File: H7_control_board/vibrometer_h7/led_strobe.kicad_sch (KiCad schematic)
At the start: 15 parts, among them Q01 NPN

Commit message: worked on audio output stuff, cleaned schematic
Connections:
- net V_USB renamed +5V
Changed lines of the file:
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@@
 	(wire
 		(pts
-			(xy 56.515 64.77) (xy 56.515 67.945)
+			(xy 55.88 65.405) (xy 55.88 67.945)
 		)
 		(stroke
@@
 	(wire
 		(pts
-			(xy 56.515 67.945) (xy 64.77 67.945)
+			(xy 55.88 67.945) (xy 64.77 67.945)
 		)
 		(stroke
@@
 	)
 	(symbol
-		(lib_id "power:+5V")
-		(at 56.515 64.77 0)
-		(mirror y)
-		(unit 1)
-		(exclude_from_sim no)
-		(in_bom yes)
-		(on_board yes)
-		(dnp no)
-		(property "Reference" "#PWR062"
-			(at 56.515 68.58 0)
-			(effects
-				(font
-					(size 1.27 1.27)
-				)
-				(hide yes)
-			)
-		)
-		(property "Value" "V_USB"
-			(at 56.515 60.96 0)
-			(effects
-				(font
-					(size 1.27 1.27)
-				)
-			)
-		)
-		(property "Footprint" ""
-			(at 56.515 64.77 0)
-			(effects
-				(font
-					(size 1.27 1.27)
-				)
-				(hide yes)
-			)
-		)
-		(property "Datasheet" ""
-			(at 56.515 64.77 0)
-			(effects
-				(font
-					(size 1.27 1.27)
-				)
-				(hide yes)
-			)
-		)
-		(property "Description" "Power symbol creates a global label with name \"+5V\""
-			(at 56.515 64.77 0)
-			(effects
-				(font
-					(size 1.27 1.27)
-				)
-				(hide yes)
-			)
-		)
-		(pin "1"
-		)
-		(instances
-			(project "vibrometer_h7"
-				(path "/18de6987-156a-4b34-871e-cbbe1d261986/4fe48606-f27d-4ac1-8d68-53a5c8e78c55"
-					(reference "#PWR062")
-					(unit 1)
-				)
-			)
-		)
-	)
-	(symbol
 		(lib_id "power:GND")
 		(at 64.77 79.375 0)
@@
 					(unit 1)
 				)
+			)
+		)
+	)
+	(symbol
+		(lib_id "power:+5V")
+		(at 55.88 65.405 0)
+		(unit 1)
+		(exclude_from_sim no)
+		(in_bom yes)
+		(on_board yes)
+		(dnp no)
+		(property "Reference" "#PWR062"
+			(at 55.88 69.215 0)
+			(effects
+				(font
+					(size 1.27 1.27)
+				)
+				(hide yes)
+			)
+		)
+		(property "Value" "+5V"
+			(at 55.88 61.468 0)
+			(effects
+				(font
+					(size 1.27 1.27)
+				)
+			)
+		)
+		(property "Footprint" ""
+			(at 55.88 65.405 0)
+			(effects
+				(font
+					(size 1.27 1.27)
+				)
+				(hide yes)
+			)
+		)
+		(property "Datasheet" ""
+			(at 55.88 65.405 0)
+			(effects
+				(font
+					(size 1.27 1.27)
+				)
+				(hide yes)
+			)
+		)
+		(property "Description" "Power symbol creates a global label with name \"+5V\""
+			(at 55.88 65.405 0)
+			(effects
+				(font
+					(size 1.27 1.27)
+				)
+				(hide yes)
+			)
+		)
+		(pin "1"
+		)
+		(instances
+			(project "vibrometer_h7"
+				(path "/18de6987-156a-4b34-871e-cbbe1d261986/4fe48606-f27d-4ac1-8d68-53a5c8e78c55"
+					(reference "#PWR062")
+					(unit 1)
+				)

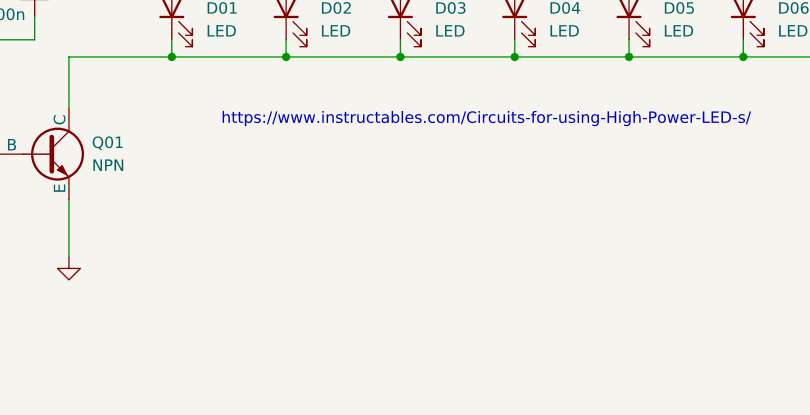
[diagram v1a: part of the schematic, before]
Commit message: added notes about LED drive component selection
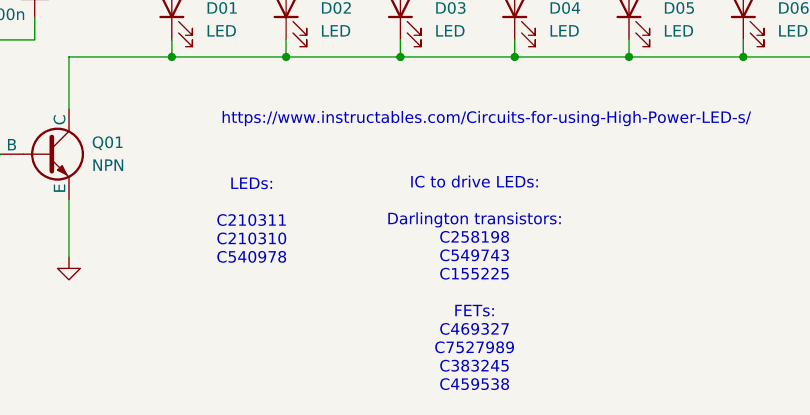
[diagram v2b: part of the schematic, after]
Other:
- note added: "IC to drive LEDs: Darlington transistors: C258198 C549743 C155225 FETs: C469327 C7527989 C383245 C459538"
- note added: "LEDs: C210311 C210310 C540978"
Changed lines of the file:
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@@
+		)
+	)
+	(text "LEDs:\n\nC210311\nC210310\nC540978\n"
+		(exclude_from_sim no)
+		(at 97.79 97.79 0)
+		(effects
+			(font
+				(size 1.27 1.27)
+			)
+		)
+	)
+	(text "IC to drive LEDs:\n\nDarlington transistors:\nC258198\nC549743\nC155225\n\nFETs:\nC469327\nC7527989\nC383245\nC459538"
+		(exclude_from_sim no)
+		(at 122.555 104.775 0)
+		(effects
+			(font
+				(size 1.27 1.27)
+			)
 		)
 	)

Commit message: started part selection
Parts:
- C01, C02: footprint (none) -> Capacitor_SMD:C_0603_1608Metric
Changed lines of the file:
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@@
 			)
 		)
-		(property "Footprint" ""
+		(property "Footprint" "Capacitor_SMD:C_0603_1608Metric"
 			(at 73.66 72.39 0)
 			(effects
@@
 			)
 		)
-		(property "Footprint" ""
+		(property "Footprint" "Capacitor_SMD:C_0603_1608Metric"
 			(at 64.77 72.39 0)
 			(effects

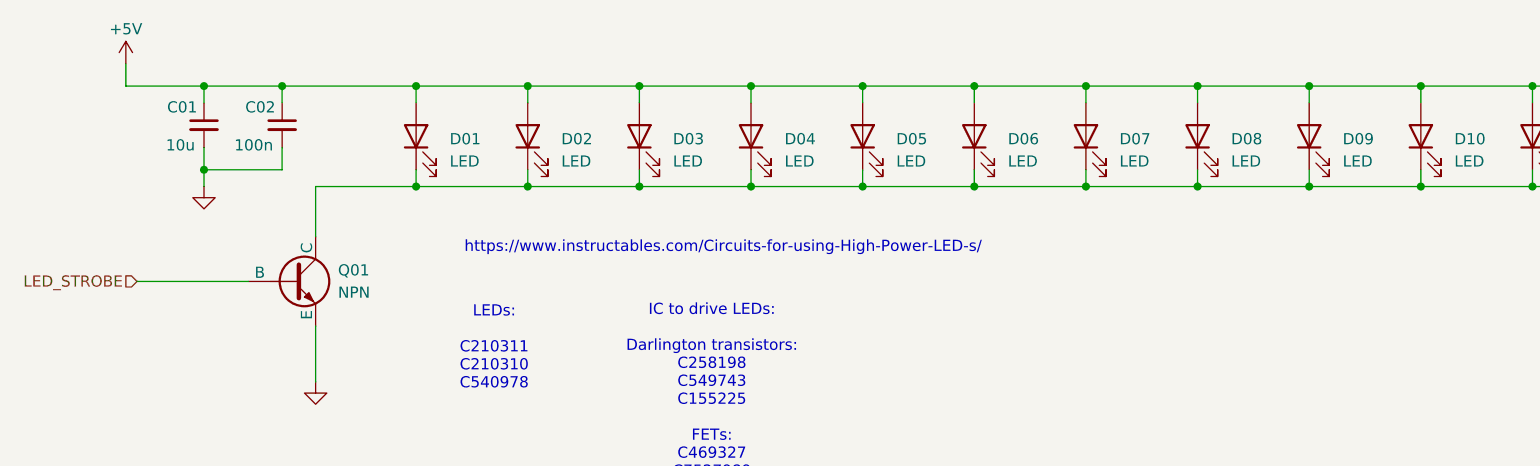
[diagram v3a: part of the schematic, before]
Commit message: component selection, headphone amp circuit specs
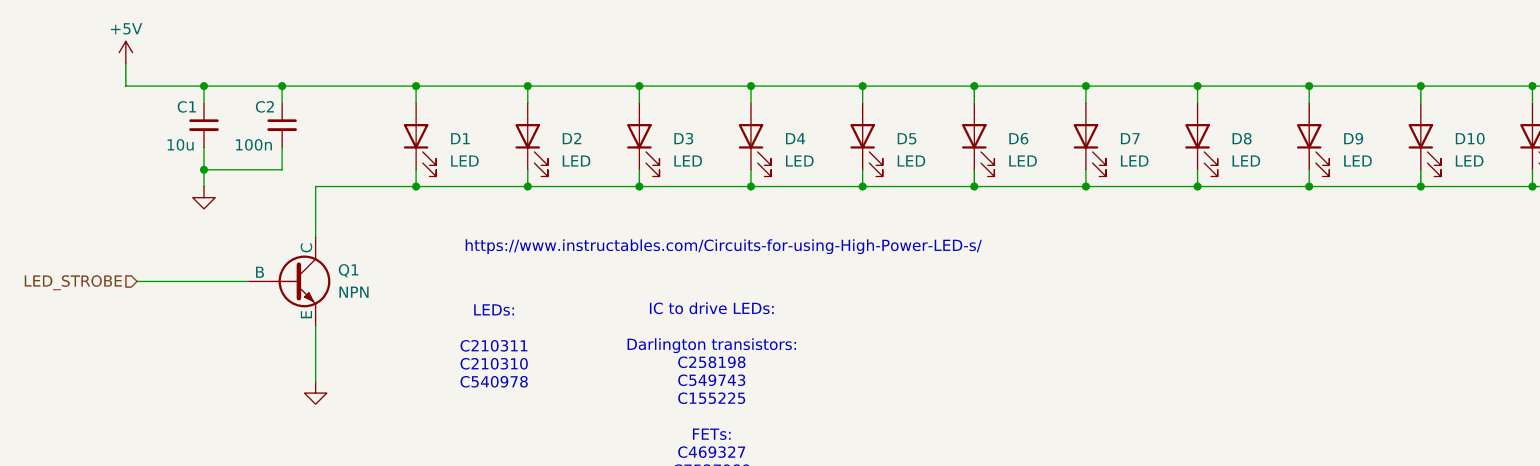
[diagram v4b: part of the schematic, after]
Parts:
- C1: renamed from C01; footprint Capacitor_SMD:C_0603_1608Metric -> Capacitor_SMD:C_0805_2012Metric; LCSC (none) -> C15850
- C2: renamed from C02; footprint Capacitor_SMD:C_0603_1608Metric -> Capacitor_SMD:C_0402_1005Metric_Pad0.74x0.62mm_HandSolder; LCSC (none) -> C307331
- renumbered D01 to D1, D02 to D2, D03 to D3, D04 to D4, D05 to D5, D06 to D6, D07 to D7, D08 to D8, D09 to D9, Q01 to Q1
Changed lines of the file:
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@@
 		(on_board yes)
 		(dnp no)
-		(property "Reference" "C02"
+		(property "Reference" "C2"
 			(at 72.898 70.358 0)
 			(effects
@@
 			)
 		)
-		(property "Footprint" "Capacitor_SMD:C_0603_1608Metric"
+		(property "Footprint" "Capacitor_SMD:C_0402_1005Metric_Pad0.74x0.62mm_HandSolder"
 			(at 73.66 72.39 0)
 			(effects
@@
 			)
 		)
-		(property "Datasheet" "~"
+		(property "Datasheet" "https://wmsc.lcsc.com/wmsc/upload/file/pdf/v2/lcsc/2304140030_Samsung-Electro-Mechanics-CL05B104KB54PNC_C307331.pdf"
 			(at 73.66 72.39 0)
 			(effects
@@
 			)
 		)
-		(property "LCSC" ""
+		(property "LCSC" "C307331"
 			(at 73.66 72.39 0)
 			(effects
@@
 			(project "vibrometer_h7"
 				(path "/18de6987-156a-4b34-871e-cbbe1d261986/4fe48606-f27d-4ac1-8d68-53a5c8e78c55"
-					(reference "C02")
+					(reference "C2")
 					(unit 1)
 				)
@@
 		(dnp no)
 		(fields_autoplaced yes)
-		(property "Reference" "D02"
+		(property "Reference" "D2"
 			(at 105.41 73.9774 90)
 			(effects
@@
 			(project "vibrometer_h7"
 				(path "/18de6987-156a-4b34-871e-cbbe1d261986/4fe48606-f27d-4ac1-8d68-53a5c8e78c55"
-					(reference "D02")
+					(reference "D2")
 					(unit 1)
 				)
@@
 		(dnp no)
 		(fields_autoplaced yes)
-		(property "Reference" "D06"
+		(property "Reference" "D6"
 			(at 156.21 73.9774 90)
 			(effects
@@
 			(project "vibrometer_h7"
 				(path "/18de6987-156a-4b34-871e-cbbe1d261986/4fe48606-f27d-4ac1-8d68-53a5c8e78c55"
-					(reference "D06")
+					(reference "D6")
 					(unit 1)
 				)
@@
 		(dnp no)
 		(fields_autoplaced yes)
-		(property "Reference" "D05"
+		(property "Reference" "D5"
 			(at 143.51 73.9774 90)
 			(effects
@@
 			(project "vibrometer_h7"
 				(path "/18de6987-156a-4b34-871e-cbbe1d261986/4fe48606-f27d-4ac1-8d68-53a5c8e78c55"
-					(reference "D05")
+					(reference "D5")
 					(unit 1)
 				)
@@
 		(on_board yes)
 		(dnp no)
-		(property "Reference" "C01"
+		(property "Reference" "C1"
 			(at 64.008 70.358 0)
 			(effects
@@
 			)
 		)
-		(property "Footprint" "Capacitor_SMD:C_0603_1608Metric"
+		(property "Footprint" "Capacitor_SMD:C_0805_2012Metric"
 			(at 64.77 72.39 0)
 			(effects
@@
 			)
 		)
-		(property "Datasheet" "~"
+		(property "Datasheet" "https://wmsc.lcsc.com/wmsc/upload/file/pdf/v2/lcsc/2304140030_Samsung-Electro-Mechanics-CL21A106KAYNNNE_C15850.pdf"
 			(at 64.77 72.39 0)
 			(effects
@@
 			)
 		)
-		(property "LCSC" ""
+		(property "LCSC" "C15850"
 			(at 64.77 72.39 0)
 			(effects
@@
 			(project "vibrometer_h7"
 				(path "/18de6987-156a-4b34-871e-cbbe1d261986/4fe48606-f27d-4ac1-8d68-53a5c8e78c55"
-					(reference "C01")
+					(reference "C1")
 					(unit 1)
 				)
@@
 		(dnp no)
 		(fields_autoplaced yes)
-		(property "Reference" "D08"
+		(property "Reference" "D8"
 			(at 181.61 73.9774 90)
 			(effects
@@
 			(project "vibrometer_h7"
 				(path "/18de6987-156a-4b34-871e-cbbe1d261986/4fe48606-f27d-4ac1-8d68-53a5c8e78c55"
-					(reference "D08")
+					(reference "D8")
 					(unit 1)
 				)
@@
 		(dnp no)
 		(fields_autoplaced yes)
-		(property "Reference" "Q01"
+		(property "Reference" "Q1"
 			(at 80.01 88.8999 0)
 			(effects
@@
 			(project ""
 				(path "/18de6987-156a-4b34-871e-cbbe1d261986/4fe48606-f27d-4ac1-8d68-53a5c8e78c55"
-					(reference "Q01")
+					(reference "Q1")
 					(unit 1)
 				)
@@
 		(dnp no)
 		(fields_autoplaced yes)
-		(property "Reference" "D04"
+		(property "Reference" "D4"
 			(at 130.81 73.9774 90)
 			(effects
@@
 			(project "vibrometer_h7"
 				(path "/18de6987-156a-4b34-871e-cbbe1d261986/4fe48606-f27d-4ac1-8d68-53a5c8e78c55"
-					(reference "D04")
+					(reference "D4")
 					(unit 1)
 				)
@@
 		(dnp no)
 		(fields_autoplaced yes)
-		(property "Reference" "D07"
+		(property "Reference" "D7"
 			(at 168.91 73.9774 90)
 			(effects
@@
 			(project "vibrometer_h7"
 				(path "/18de6987-156a-4b34-871e-cbbe1d261986/4fe48606-f27d-4ac1-8d68-53a5c8e78c55"
-					(reference "D07")
+					(reference "D7")
 					(unit 1)
 				)
@@
 		(dnp no)
 		(fields_autoplaced yes)
-		(property "Reference" "D09"
+		(property "Reference" "D9"
 			(at 194.31 73.9774 90)
 			(effects
@@
 			(project "vibrometer_h7"
 				(path "/18de6987-156a-4b34-871e-cbbe1d261986/4fe48606-f27d-4ac1-8d68-53a5c8e78c55"
-					(reference "D09")
+					(reference "D9")
 					(unit 1)
 				)
@@
 		(dnp no)
 		(fields_autoplaced yes)
-		(property "Reference" "D01"
+		(property "Reference" "D1"
 			(at 92.71 73.9774 90)
 			(effects
@@
 			(project ""
 				(path "/18de6987-156a-4b34-871e-cbbe1d261986/4fe48606-f27d-4ac1-8d68-53a5c8e78c55"
-					(reference "D01")
+					(reference "D1")
 					(unit 1)
 				)
@@
 		(dnp no)
 		(fields_autoplaced yes)
-		(property "Reference" "D03"
+		(property "Reference" "D3"
 			(at 118.11 73.9774 90)
 			(effects
@@
 			(project "vibrometer_h7"
 				(path "/18de6987-156a-4b34-871e-cbbe1d261986/4fe48606-f27d-4ac1-8d68-53a5c8e78c55"
-					(reference "D03")
-					(unit 1)
-				)
+					(reference "D3")
+					(unit 1)
+				)

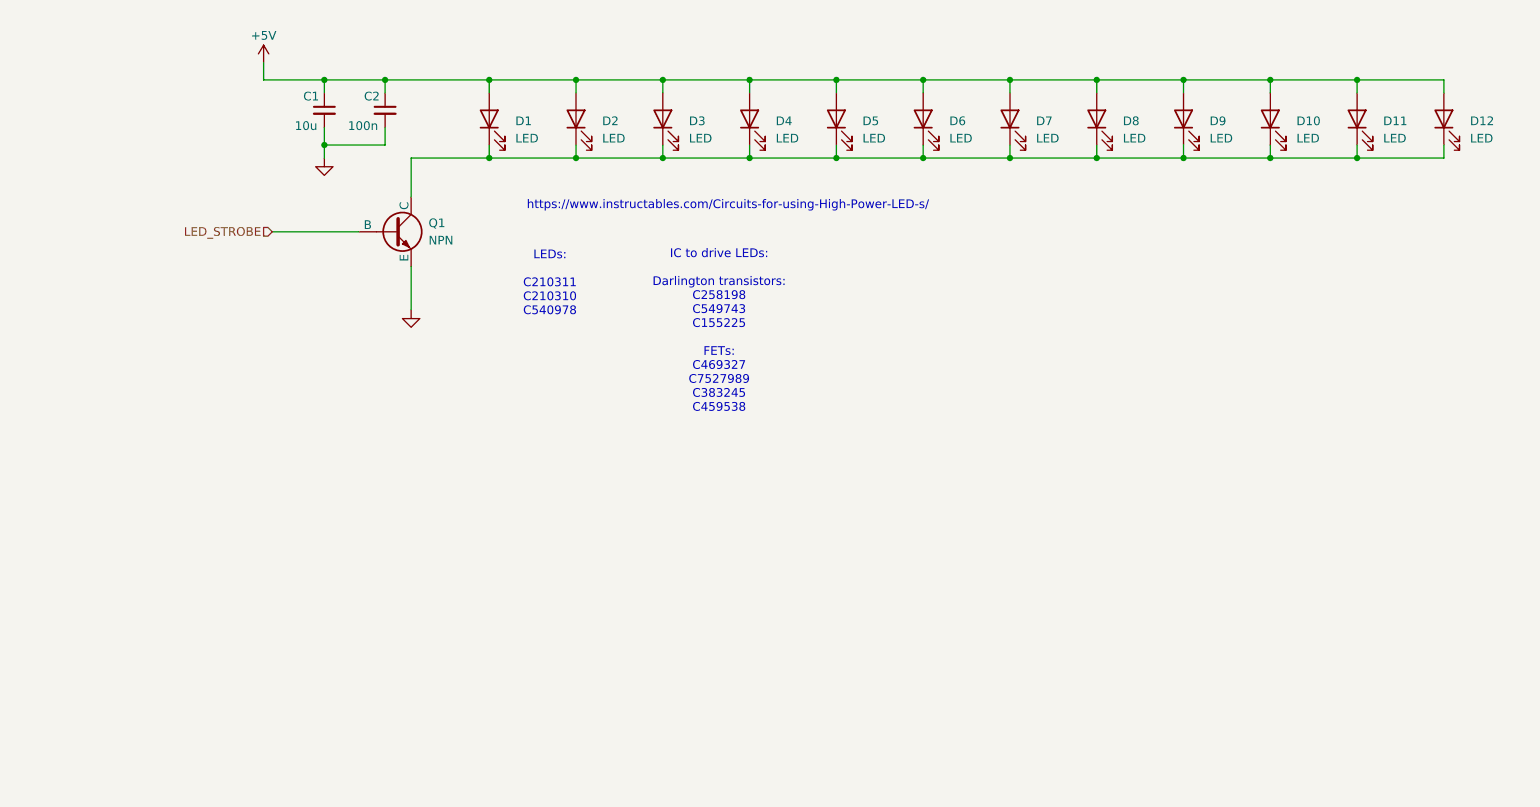
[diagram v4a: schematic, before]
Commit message: updated reference designator naming
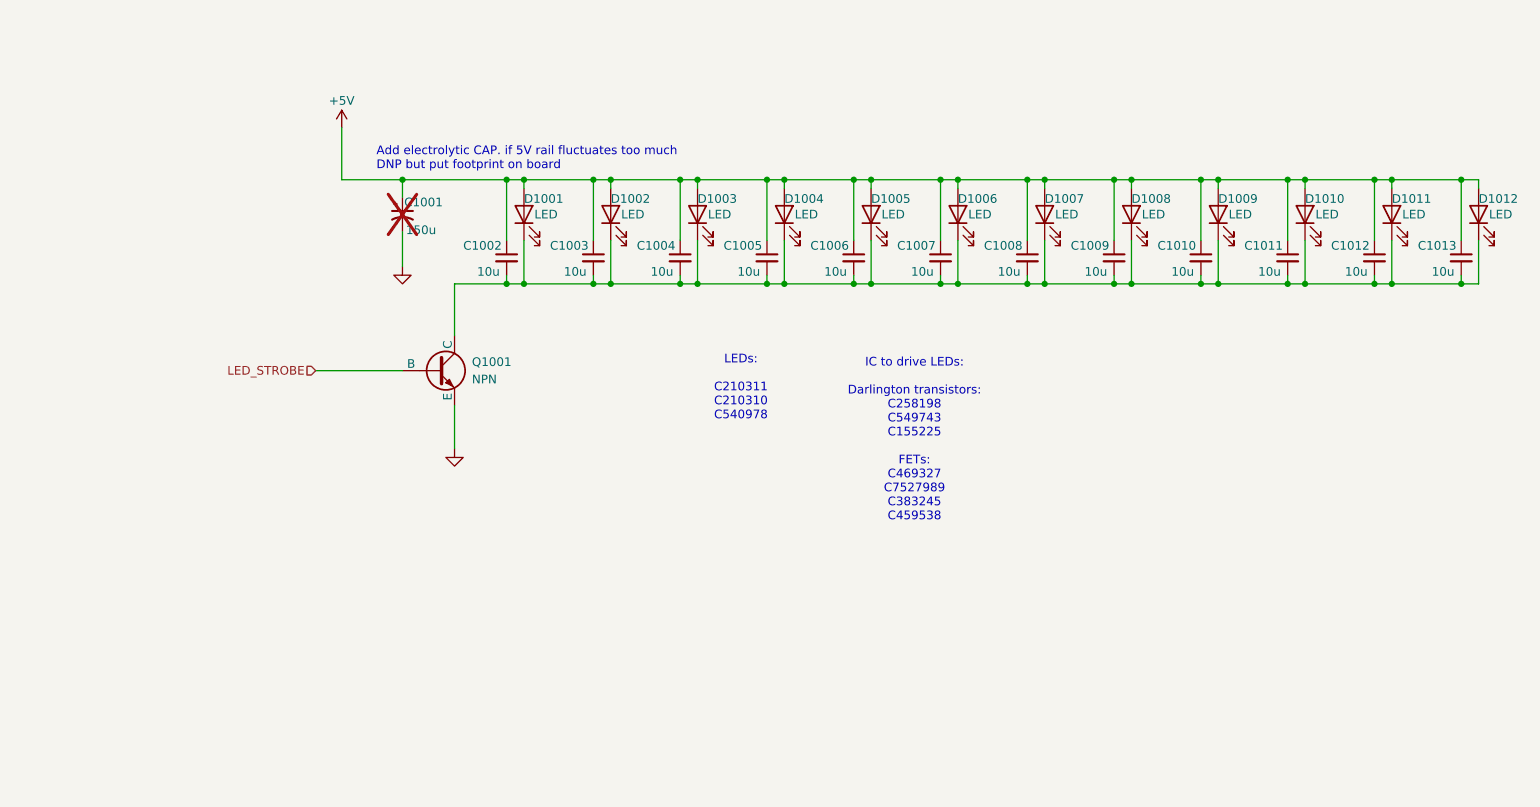
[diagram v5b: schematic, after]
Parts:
- removed C1: 10u, Capacitor_SMD:C_0805_2012Metric, symbol Device:C_Small
- removed C2: 100n, Capacitor_SMD:C_0402_1005Metric_Pad0.74x0.62mm_HandSolder, symbol Device:C_Small
- removed D10, D11, D12, D2, D3, D4, D5, D6, D7, D8, D9: LED, symbol Device:LED
- added C1001: 150u, symbol Device:C_Polarized_Small_US
- added C1002, C1003, C1004, C1005, C1006, C1007, C1008, C1009, C1010, C1011, C1012, C1013: 10u, symbol Device:C_Small
- added D1002, D1003, D1004, D1005, D1006, D1007, D1008, D1009, D1010, D1011, D1012: LED, symbol Device:LED
- renumbered D1 to D1001, Q1 to Q1001
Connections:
- net +5V: now also C1001.1, C1002.1, C1003.1, C1004.1, C1005.1, C1006.1, C1007.1, C1008.1, C1009.1, C1010.1, C1011.1, C1012.1, C1013.1, D1002.2 (A), D1003.2 (A), D1004.2 (A), D1005.2 (A), D1006.2 (A), D1007.2 (A), D1008.2 (A), D1009.2 (A), D1010.2 (A), D1011.2 (A), D1012.2 (A)
- net GND: now also C1001.2
- net at D1001.1 (K), Q1001.1 (C): now also C1002.2, C1003.2, C1004.2, C1005.2, C1006.2, C1007.2, C1008.2, C1009.2, C1010.2, C1011.2, C1012.2, C1013.2, D1002.1 (K), D1003.1 (K), D1004.1 (K), D1005.1 (K), D1006.1 (K), D1007.1 (K), D1008.1 (K), D1009.1 (K), D1010.1 (K), D1011.1 (K), D1012.1 (K)
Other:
- note added: "Add electrolytic CAP. if 5V rail fluctuates too much DNP but put footprint on board"
- note removed: "https://www.instructables.com/Circuits-for-using-High-Power-LED-s/"
- moved on the sheet: D1001, Q1001
